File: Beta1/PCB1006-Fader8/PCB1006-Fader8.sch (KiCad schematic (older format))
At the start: 22 parts, among them U1000 MCP3008T-I/SL

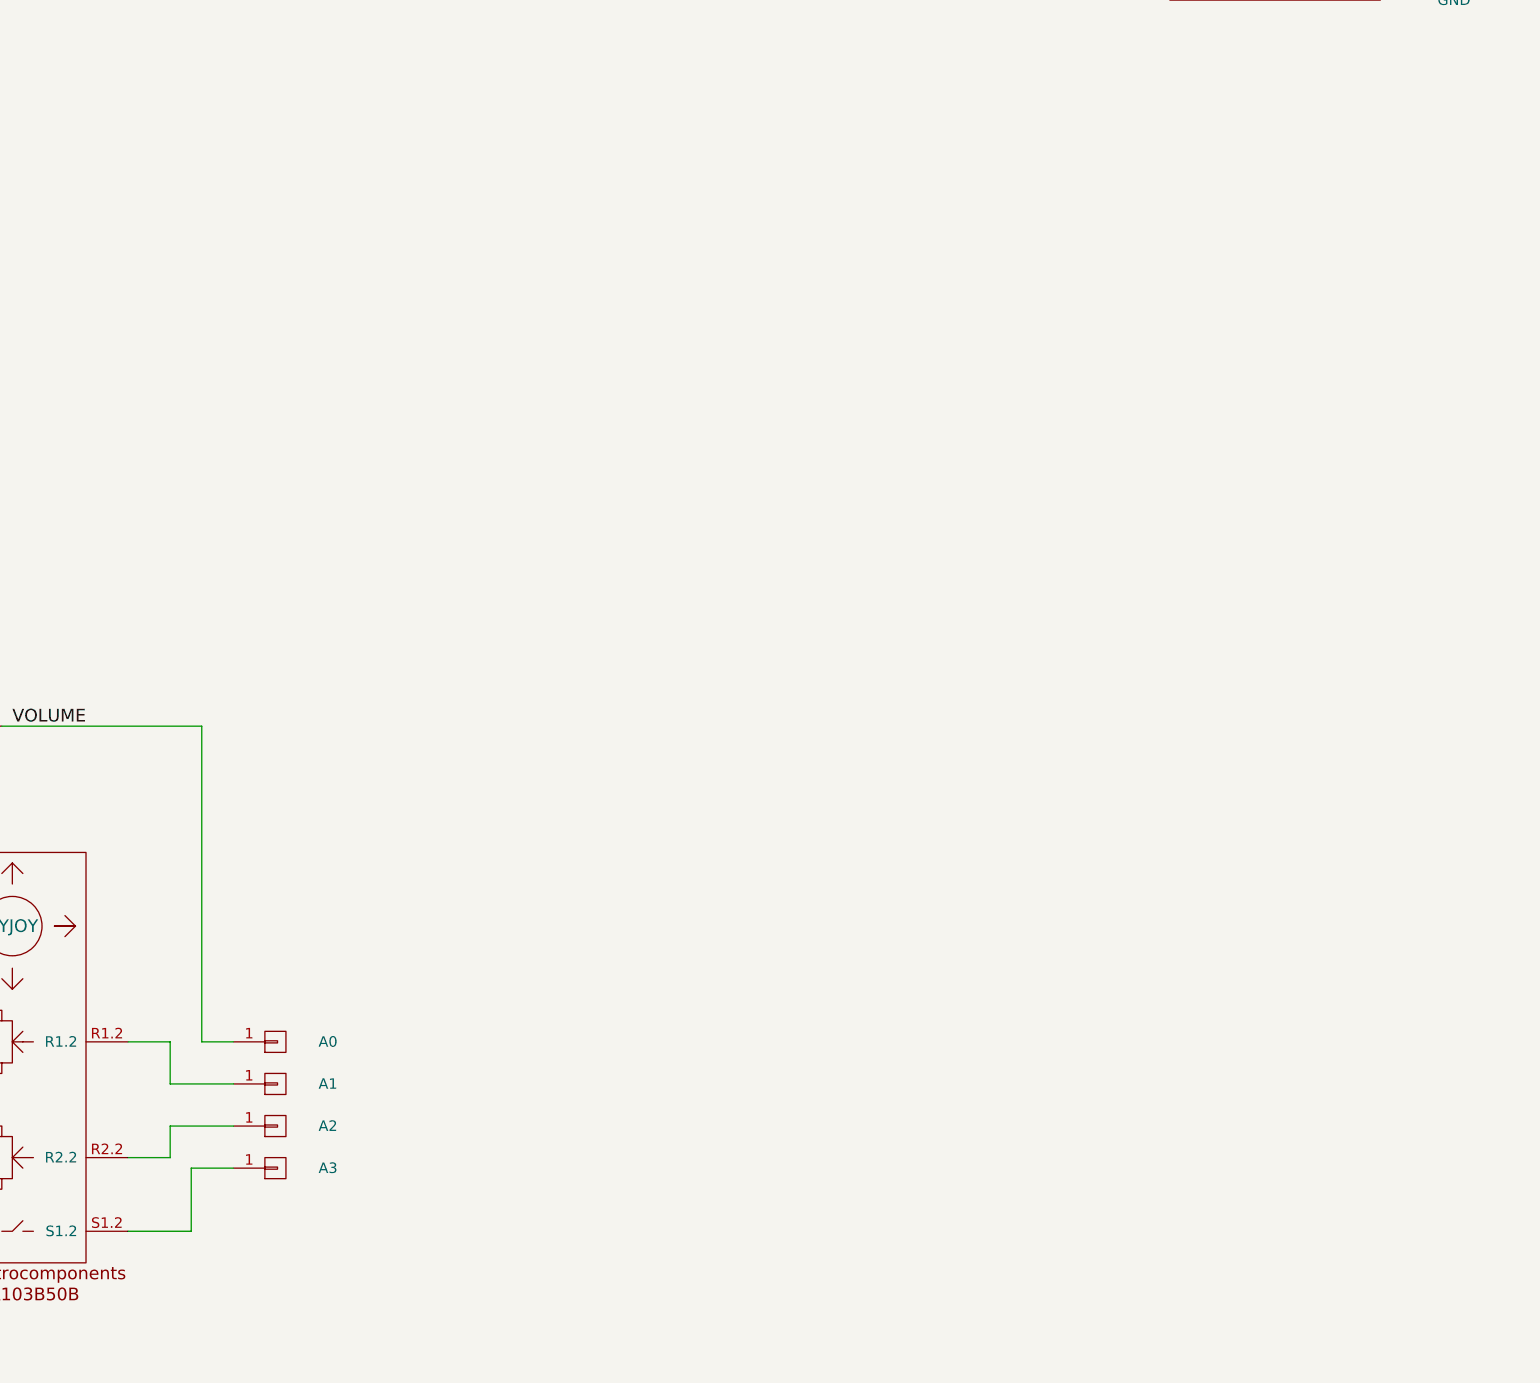
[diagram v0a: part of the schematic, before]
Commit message: Added USB-K connector
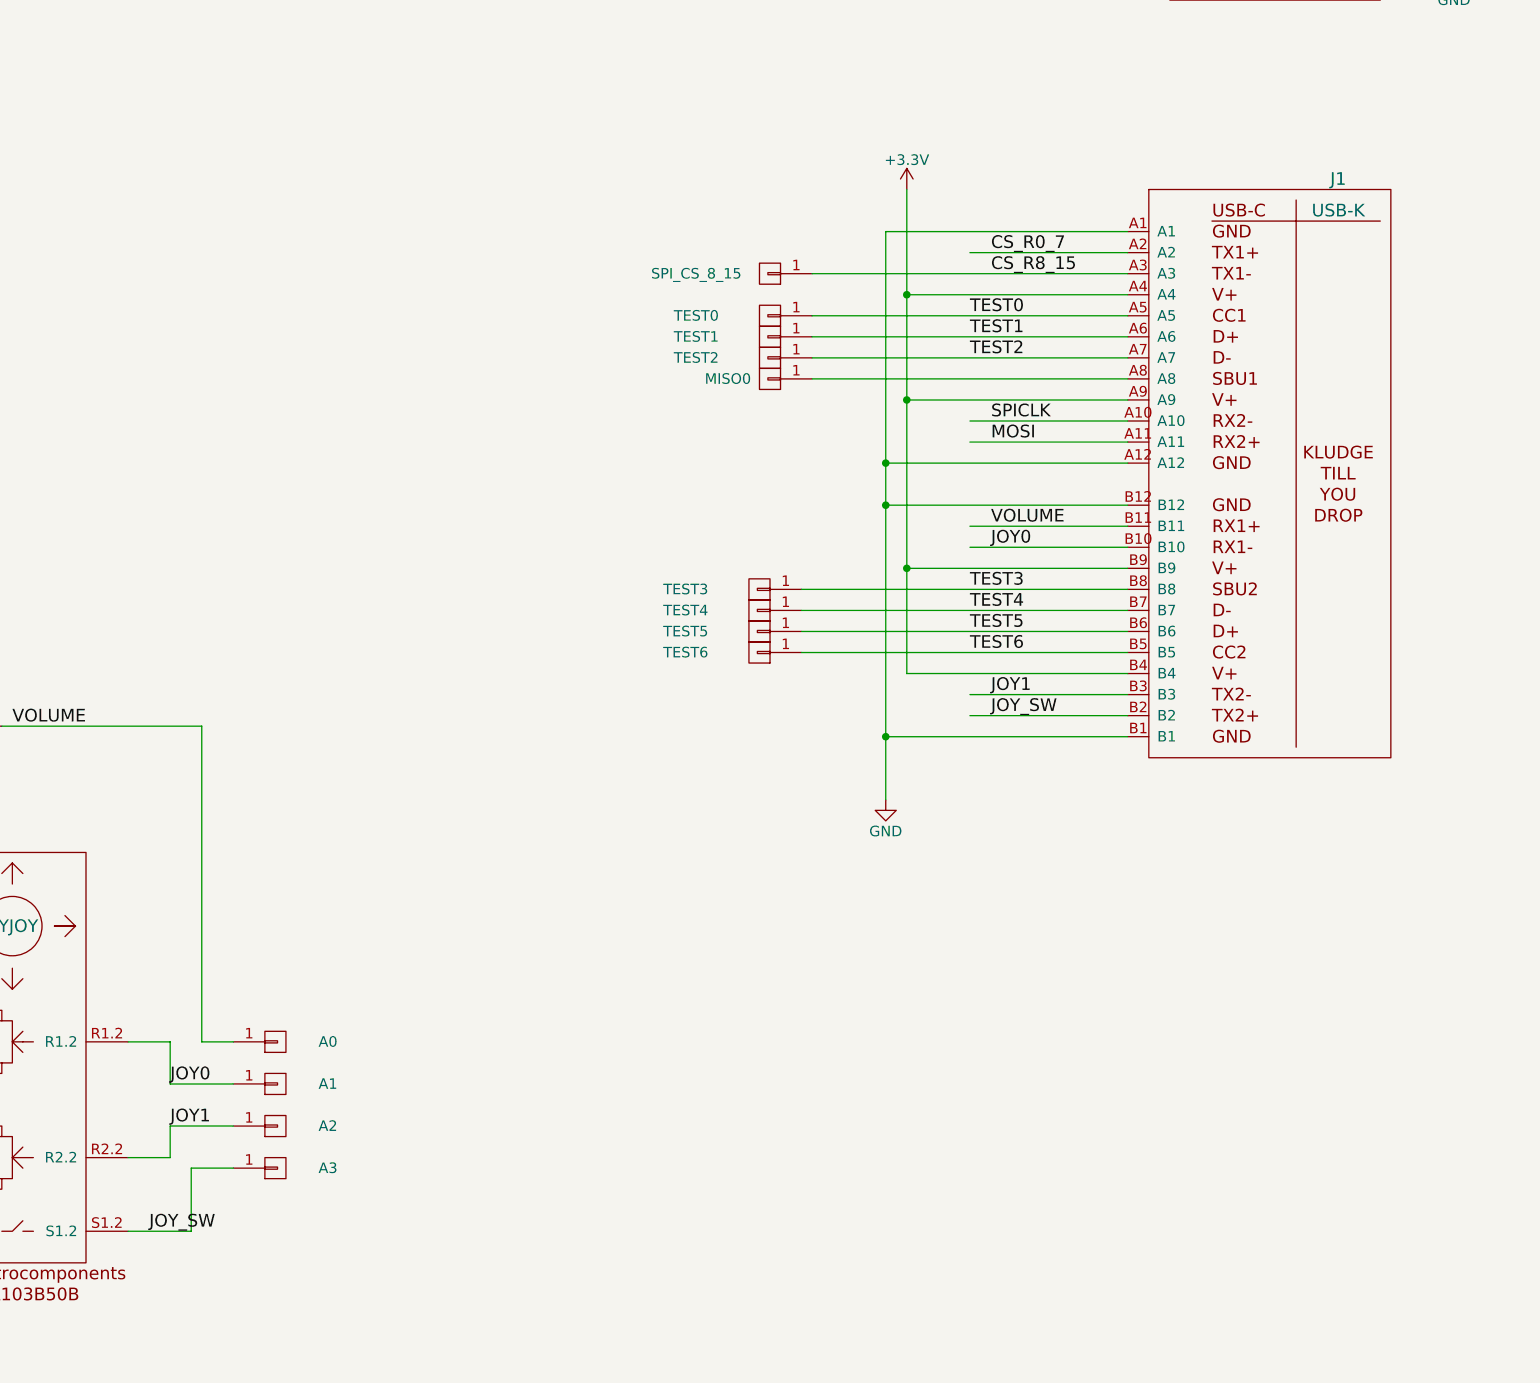
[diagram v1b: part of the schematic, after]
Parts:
- added J1: USB-K, Liberry:USB-K_12401610E4_2A, symbol USB-K
- added MISO0, SPI_CS_8_15, TEST0, TEST1, TEST2, TEST3, TEST4, TEST5, TEST6: CONN_01X01, Liberry:TH_0.1_1x2_Jumper, symbol CONN_01X01
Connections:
- net labels added: CS_R8_15, JOY0, JOY1, JOY_SW, TEST0, TEST1, TEST2, TEST3, TEST4, TEST5, TEST6
- wire segments 68 -> 94
